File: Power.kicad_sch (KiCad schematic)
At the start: 0 parts

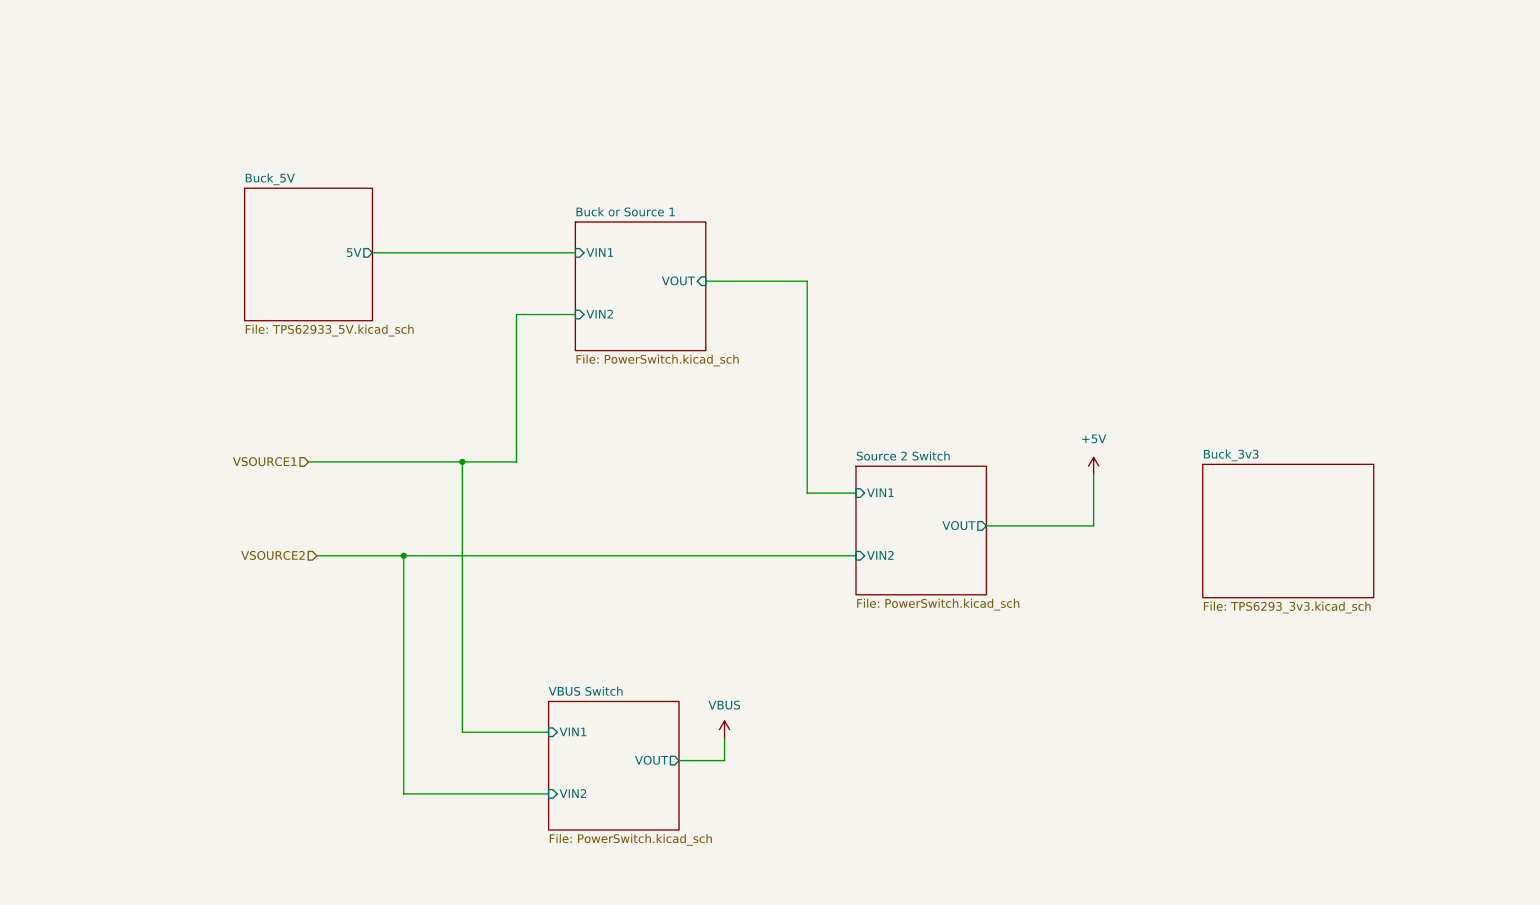
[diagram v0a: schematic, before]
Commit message: fixing sheet numbers and adding schematic PDF
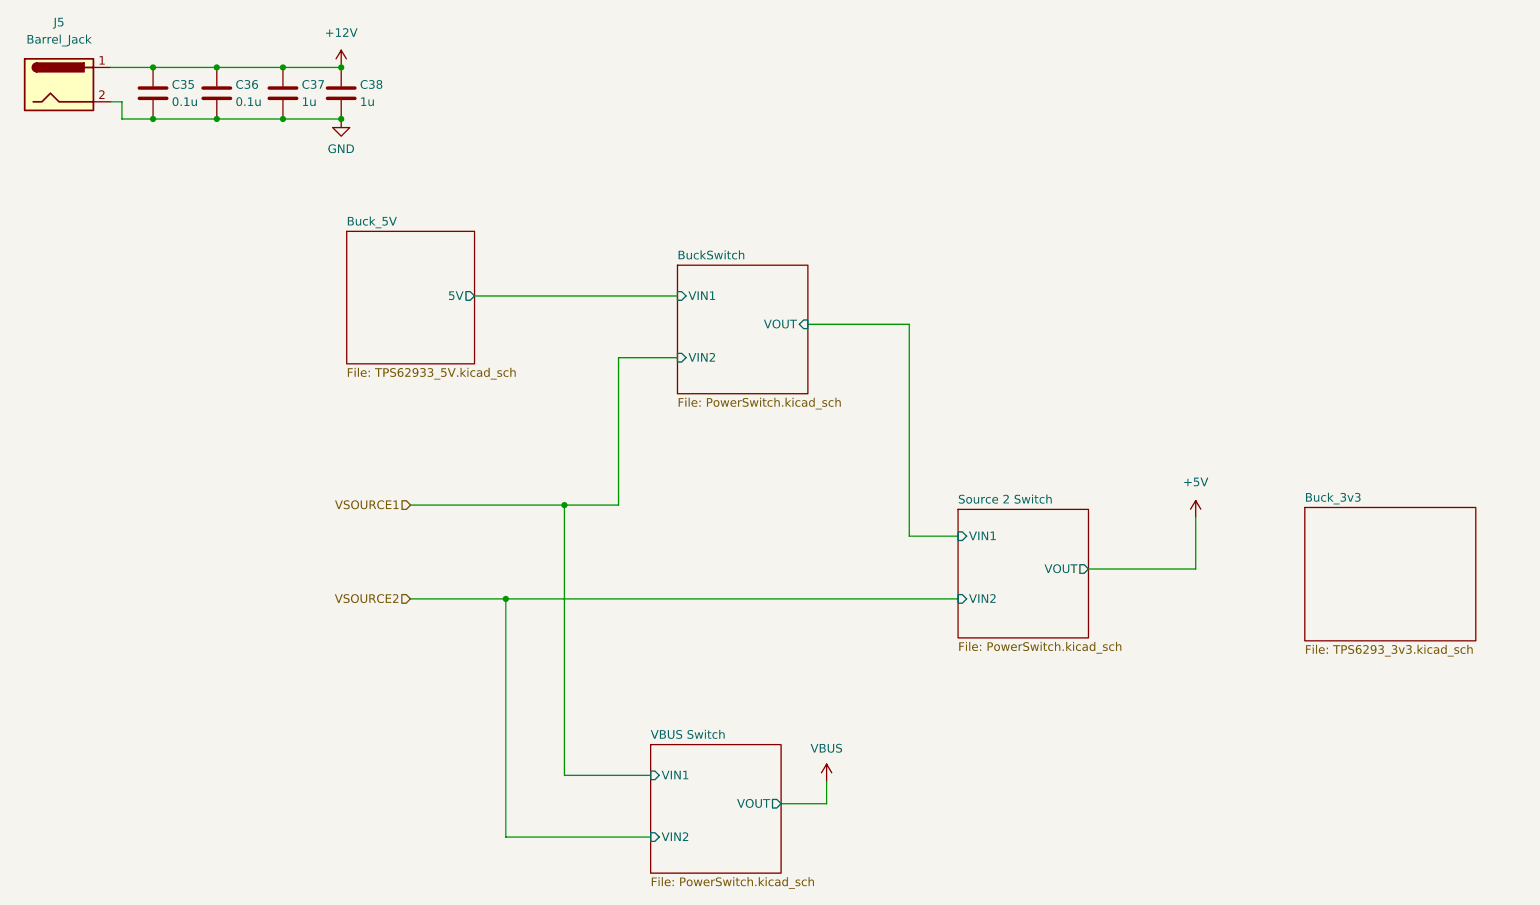
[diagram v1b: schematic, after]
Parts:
- added C35, C36: 0.1u, symbol Device:C
- added C37, C38: 1u, symbol Device:C
- added J5: Barrel_Jack, symbol Connector:Barrel_Jack
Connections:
- new net +12V: C35.1, C36.1, C37.1, C38.1, J5.1
- new net GND: C35.2, C36.2, C37.2, C38.2, J5.2
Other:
- sheet Buck or Source 1 renamed BuckSwitch

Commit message: Fixing ERC
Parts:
- renumbered C35 to C31, C36 to C32, C37 to C33, C38 to C34, J5 to J7
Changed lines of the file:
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@@
   (symbol (lib_id "Connector:Barrel_Jack") (at 26.4668 30.1498 0) (unit 1)
     (in_bom yes) (on_board yes) (fields_autoplaced)
-    (property "Reference" "J5" (id 0) (at 26.4668 20.955 0))
+    (property "Reference" "J7" (id 0) (at 26.4668 20.955 0))
     (property "Value" "Barrel_Jack" (id 1) (at 26.4668 23.495 0))
     (property "Footprint" "" (id 2) (at 27.7368 31.1658 0)
@@
   (symbol (lib_id "Device:C") (at 40.3606 31.4198 0) (unit 1)
     (in_bom yes) (on_board yes)
-    (property "Reference" "C35" (id 0) (at 43.1292 30.1752 0)
+    (property "Reference" "C31" (id 0) (at 43.1292 30.1752 0)
       (effects (font (size 1.27 1.27)) (justify left))
     )
@@
   (symbol (lib_id "power:GND") (at 68.1736 35.2298 0) (unit 1)
     (in_bom yes) (on_board yes) (fields_autoplaced)
-    (property "Reference" "#PWR050" (id 0) (at 68.1736 41.5798 0)
+    (property "Reference" "#PWR056" (id 0) (at 68.1736 41.5798 0)
       (effects (font (size 1.27 1.27)) hide)
     )
@@
   (symbol (lib_id "Device:C") (at 59.563 31.4198 0) (unit 1)
     (in_bom yes) (on_board yes)
-    (property "Reference" "C37" (id 0) (at 62.3316 30.1752 0)
+    (property "Reference" "C33" (id 0) (at 62.3316 30.1752 0)
       (effects (font (size 1.27 1.27)) (justify left))
     )
@@
   (symbol (lib_id "Device:C") (at 49.784 31.4198 0) (unit 1)
     (in_bom yes) (on_board yes)
-    (property "Reference" "C36" (id 0) (at 52.5526 30.1752 0)
+    (property "Reference" "C32" (id 0) (at 52.5526 30.1752 0)
       (effects (font (size 1.27 1.27)) (justify left))
     )
@@
   (symbol (lib_id "power:+12V") (at 68.1736 27.6098 0) (unit 1)
     (in_bom yes) (on_board yes) (fields_autoplaced)
-    (property "Reference" "#PWR049" (id 0) (at 68.1736 31.4198 0)
+    (property "Reference" "#PWR055" (id 0) (at 68.1736 31.4198 0)
       (effects (font (size 1.27 1.27)) hide)
     )
@@
   (symbol (lib_id "power:+5V") (at 194.4878 94.1832 0) (unit 1)
     (in_bom yes) (on_board yes) (fields_autoplaced)
-    (property "Reference" "#PWR052" (id 0) (at 194.4878 97.9932 0)
+    (property "Reference" "#PWR058" (id 0) (at 194.4878 97.9932 0)
       (effects (font (size 1.27 1.27)) hide)
     )
@@
   (symbol (lib_id "Device:C") (at 68.1736 31.4198 0) (unit 1)
     (in_bom yes) (on_board yes)
-    (property "Reference" "C38" (id 0) (at 70.9422 30.1752 0)
+    (property "Reference" "C34" (id 0) (at 70.9422 30.1752 0)
       (effects (font (size 1.27 1.27)) (justify left))
     )
@@
   (symbol (lib_id "power:VBUS") (at 139.9286 133.1468 0) (unit 1)
     (in_bom yes) (on_board yes) (fields_autoplaced)
-    (property "Reference" "#PWR051" (id 0) (at 139.9286 136.9568 0)
+    (property "Reference" "#PWR057" (id 0) (at 139.9286 136.9568 0)
       (effects (font (size 1.27 1.27)) hide)
     )

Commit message: Pushing what i have now
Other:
- removed sheet BuckSwitch
- removed sheet Source 2 Switch
- removed sheet VBUS Switch
- sheet Buck_5V ports: added none; removed 5V
